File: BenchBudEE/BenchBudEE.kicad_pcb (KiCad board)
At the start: 4 copper layers, 165.1 x 63.5 mm, 0 parts

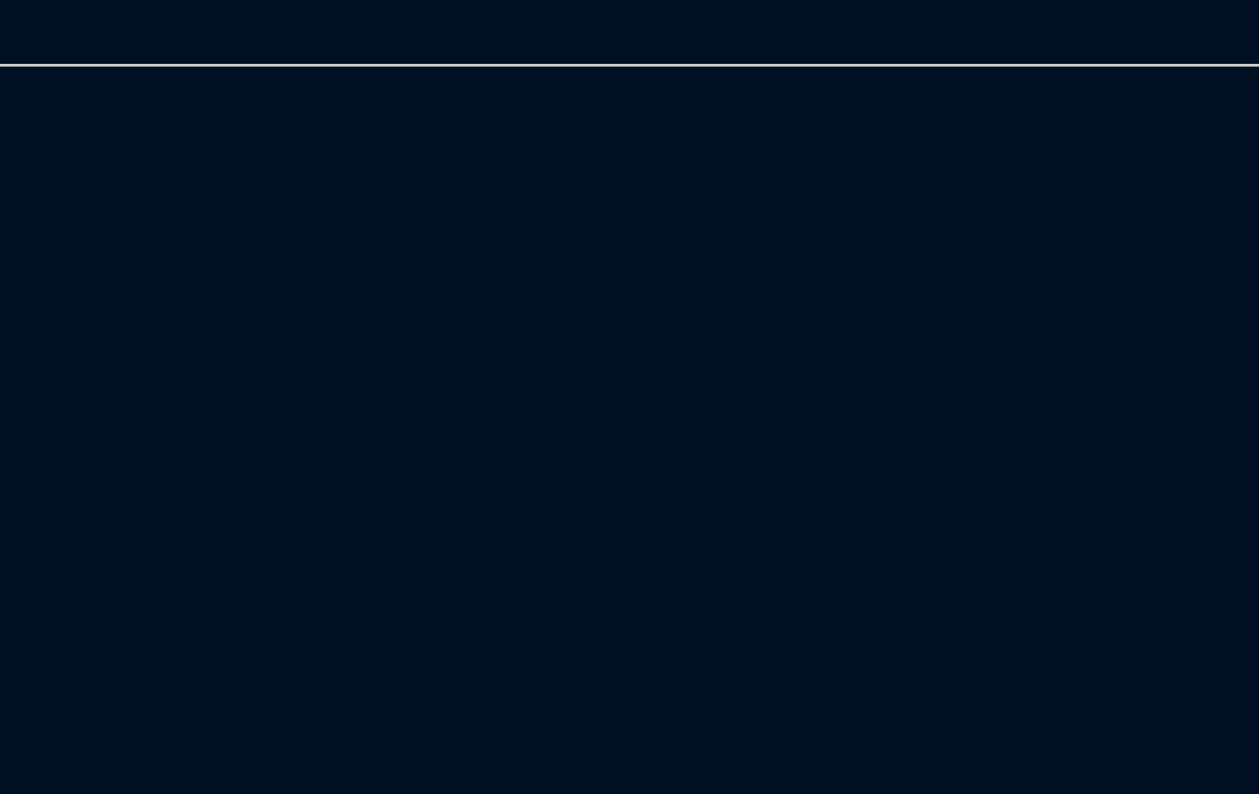
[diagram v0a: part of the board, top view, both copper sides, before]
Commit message: Associating and Placing the Relay Module
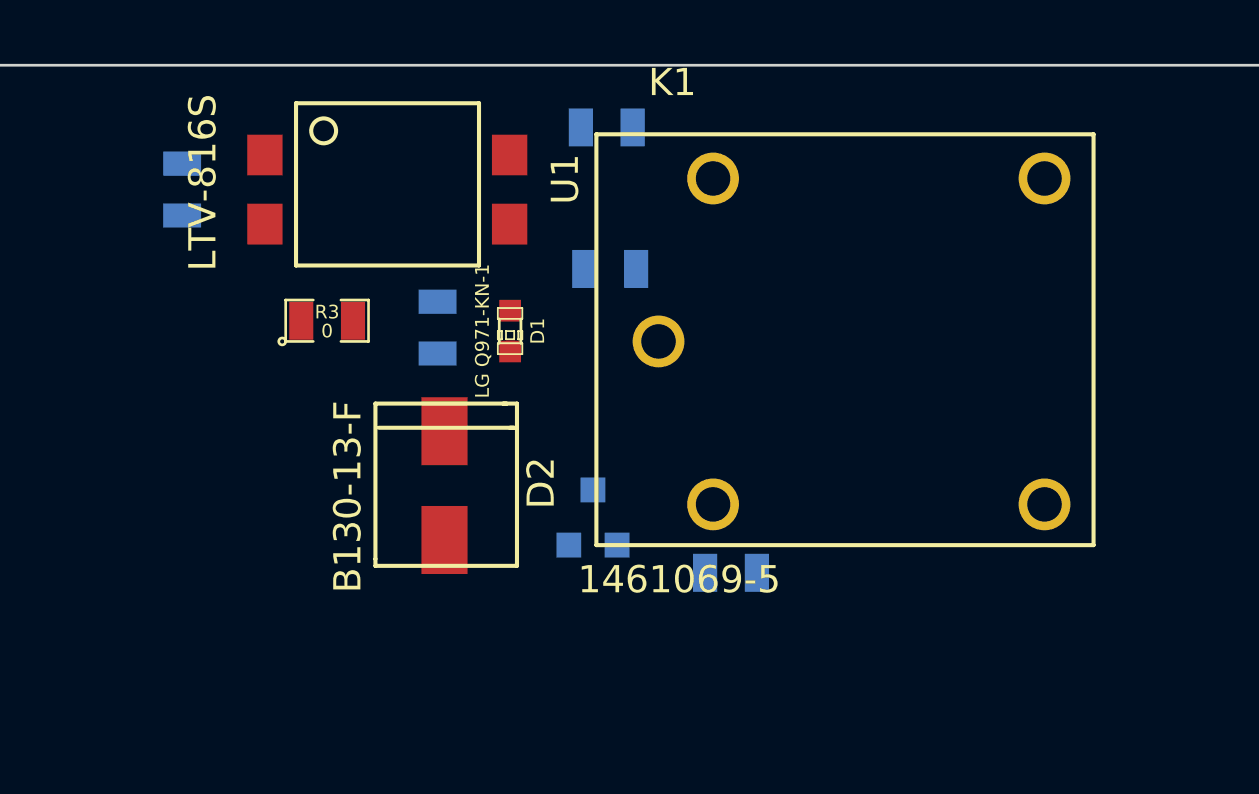
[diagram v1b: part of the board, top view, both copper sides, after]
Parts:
- added D1: LG Q971-KN-1, LED-0603, F.Cu at (252.6, 107.8)
- added D2: B130-13-F, SMA, F.Cu at (250.2, 111.5)
- added K1: 1461069-5, TE-SPDT, F.Cu at (258.1, 108.2)
- added Q1: 2N3904, SOT23EBC, B.Cu at (255.7, 114.7)
- added R1: 500, SM0805, B.Cu at (240.5, 102.6)
- added R2: 200, SM0805, B.Cu at (249.9, 107.7)
- added R3: 0, SM0805, F.Cu at (245.9, 107.4)
- added R4: 100, SM0805, B.Cu at (256.3, 105.5)
- added R5: 0, SM0805, B.Cu at (256.2, 100.3)
- added R6: 0, SM0805, B.Cu at (260.7, 116.7)
- added U1: LTV-816S, 4-SMD, F.Cu at (243.6, 101.3)

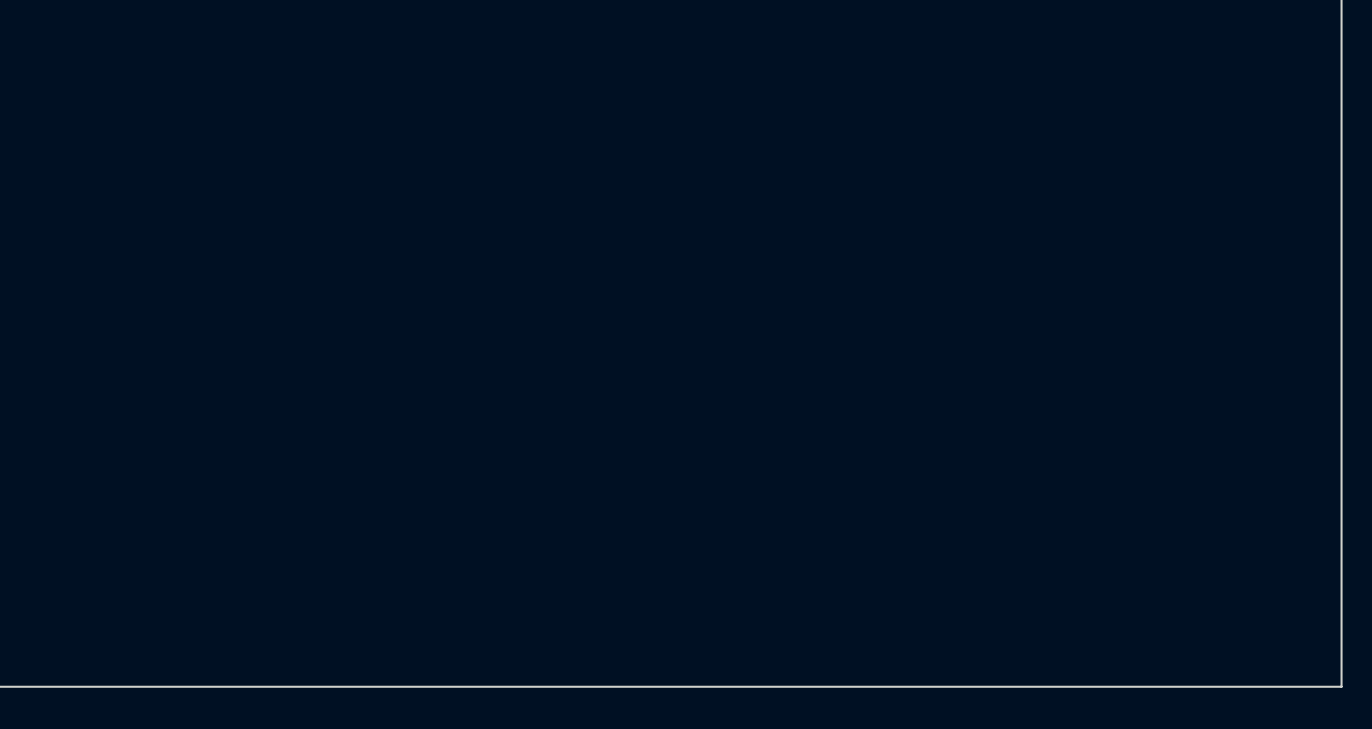
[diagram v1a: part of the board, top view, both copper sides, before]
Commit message: Associating and Placingthe Thermocouple Module
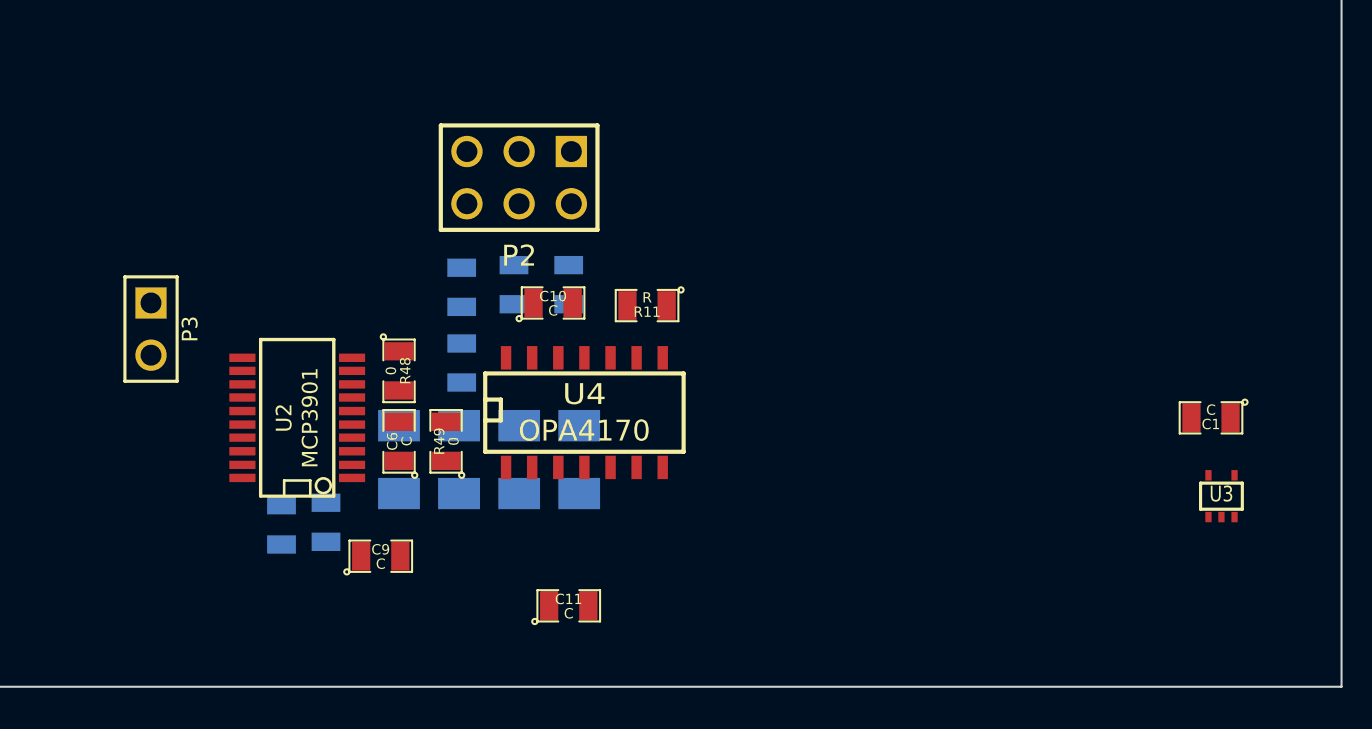
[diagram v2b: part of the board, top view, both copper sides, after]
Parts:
- added C1: C, SM0805, F.Cu at (284.0, 148.5)
- added C10: C, SM0805, F.Cu at (252.0, 142.9)
- added C11: C, SM0805, F.Cu at (252.7, 157.6)
- added C6: C, SM0805, F.Cu at (244.5, 149.6)
- added C7: C, SM0805, B.Cu at (238.8, 153.7)
- added C8: C, SM0805, B.Cu at (240.9, 153.5)
- added C9: C, SM0805, F.Cu at (243.6, 155.2)
- added P2: CONN_3X2, pin_array_3x2, F.Cu at (250.3, 136.8)
- added P3: CONN_2, PIN_ARRAY_2X1, F.Cu at (232.4, 144.1)
- added R10: R, SM1206, B.Cu at (253.2, 150.5)
- added R11: R, SM0805, F.Cu at (256.5, 143.0)
- added R12: R, SM0805, B.Cu at (252.7, 142.0)
- added R13: R, SM0805, B.Cu at (247.5, 145.8)
- added R44: R, SM0805, B.Cu at (247.5, 142.1)
- added R45: R, SM0805, B.Cu at (250.1, 142.0)
- added R48: 0, SM0805, F.Cu at (244.5, 146.2)
- added R49: 0, SM0805, F.Cu at (246.8, 149.6)
- added R7: R, SM1206, B.Cu at (244.5, 150.5)
- added R8: R, SM1206, B.Cu at (247.4, 150.5)
- added R9: R, SM1206, B.Cu at (250.3, 150.5)
- added U2: MCP3901, SSOP20, F.Cu at (239.5, 148.5)
- added U3: LMT84, SOT353, F.Cu at (284.5, 152.3)
- added U4: OPA4170, SO14E, F.Cu at (253.5, 148.1)

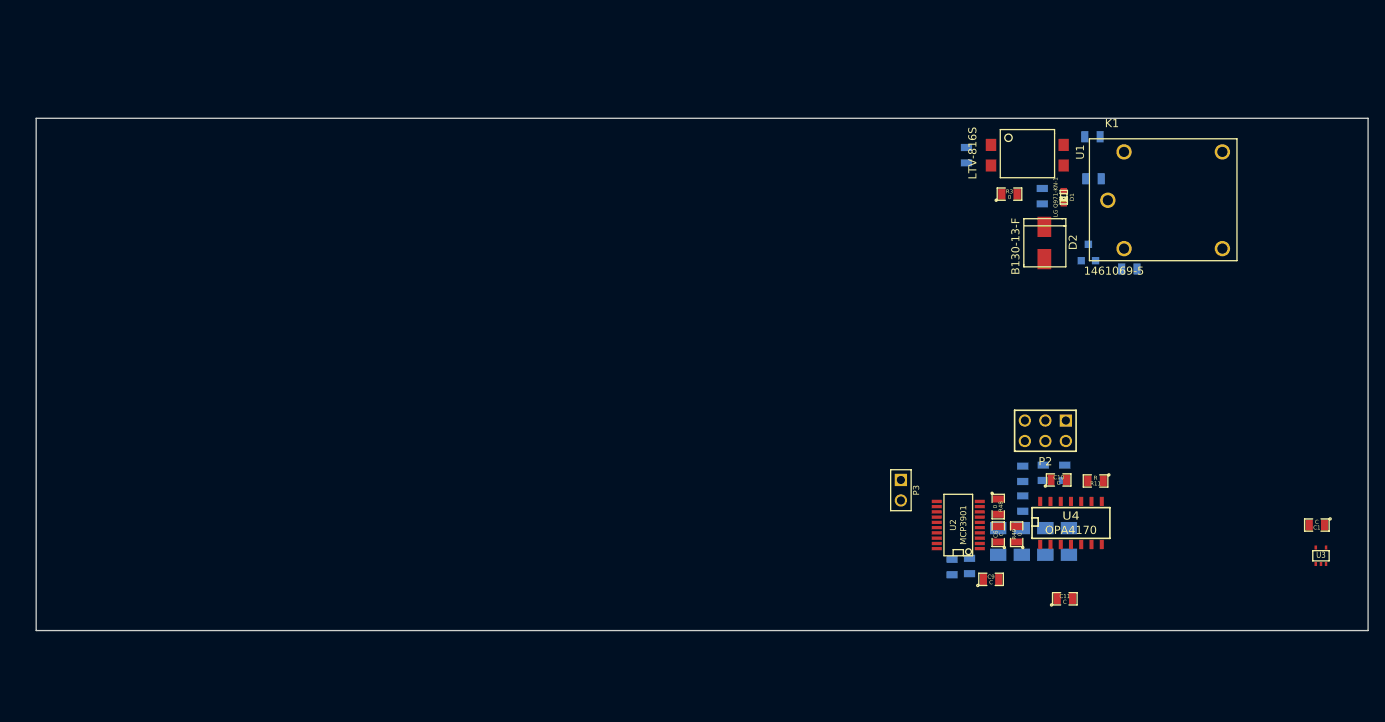
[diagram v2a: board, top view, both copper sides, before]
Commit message: Associating and Placing the Terminal Block Module
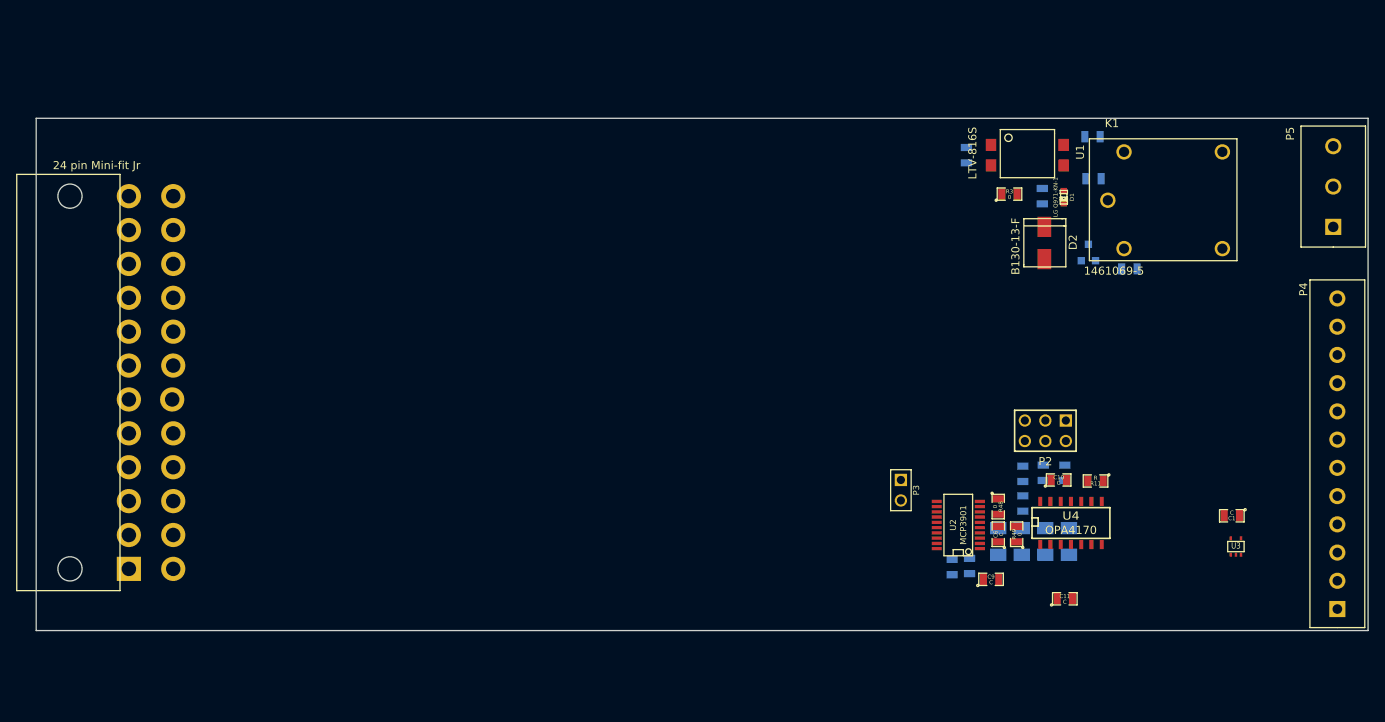
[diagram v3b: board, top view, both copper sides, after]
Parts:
- added P1: 24 pin Mini-fit Jr, ATX_Header, F.Cu at (129.4, 107.7)
- added P4: 12 pin terminal block, 12_Pin_TB, F.Cu at (286.5, 158.9)
- added P5: 3 Pin TB, 3_Pin_TB, F.Cu at (286.0, 111.5)
- moved C1 10.6 mm to (273.4, 147.3)
- moved U3 10.6 mm to (273.9, 151.1)
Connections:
- K1 pad 1: (no net) -> /Relay/RELAY_COM
- K1 pad 3: (no net) -> /Relay/RELAY_NO
- K1 pad 4: (no net) -> /Relay/RELAY_NC

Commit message: Associating and Placing Arduino Block Module
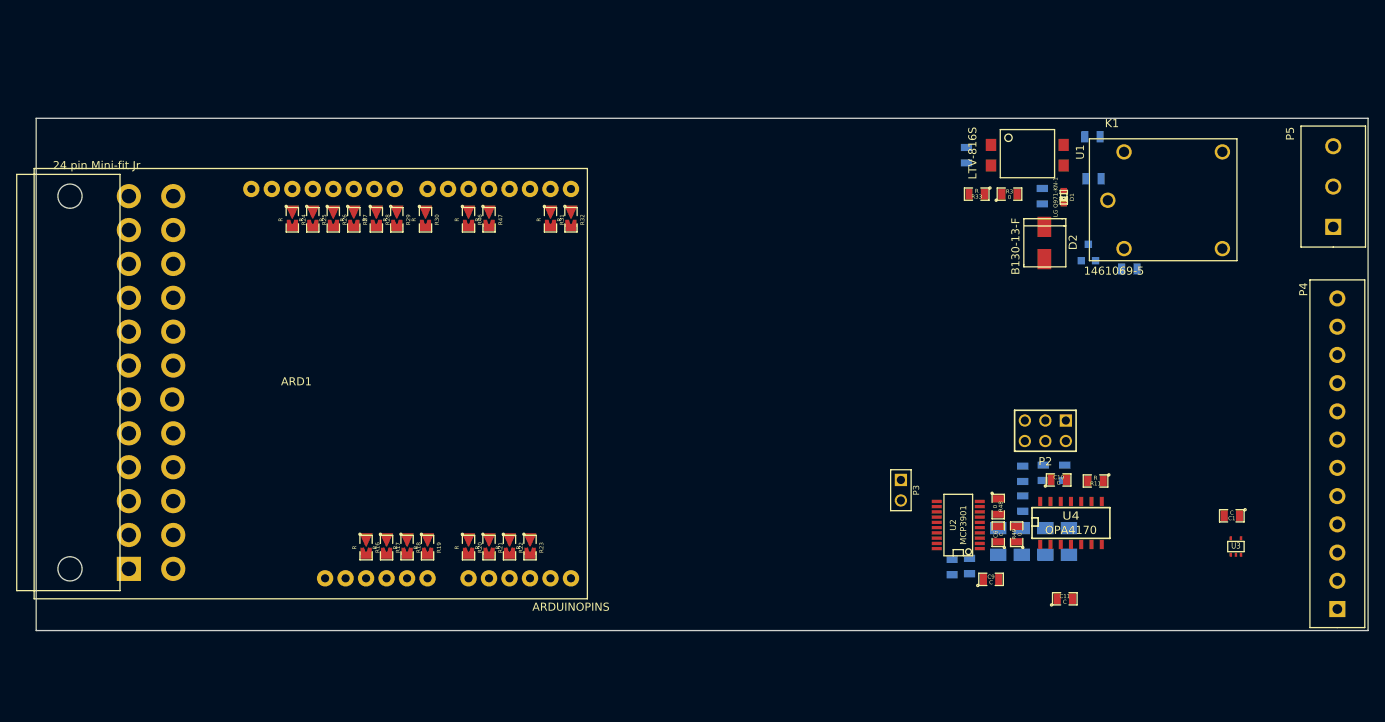
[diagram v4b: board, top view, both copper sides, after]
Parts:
- added ARD1: ARDUINOPINS, Arduino, F.Cu at (157.5, 130.7)
- added R16: R, SM0805-blob, F.Cu at (166.1, 151.3)
- added R17: R, SM0805-blob, F.Cu at (168.7, 151.3)
- added R18: R, SM0805-blob, F.Cu at (171.2, 151.3)
- added R19: R, SM0805-blob, F.Cu at (173.7, 151.3)
- added R20: R, SM0805-blob, F.Cu at (178.8, 151.3)
- added R21: R, SM0805-blob, F.Cu at (181.4, 151.3)
- added R22: R, SM0805-blob, F.Cu at (183.9, 151.3)
- added R23: R, SM0805-blob, F.Cu at (186.4, 151.3)
- added R24: R, SM0805-blob, F.Cu at (157.0, 110.6)
- added R25: R, SM0805-blob, F.Cu at (159.5, 110.6)
- added R26: R, SM0805-blob, F.Cu at (162.1, 110.6)
- added R27: R, SM0805-blob, F.Cu at (164.6, 110.6)
- added R28: R, SM0805-blob, F.Cu at (167.4, 110.6)
- added R29: R, SM0805-blob, F.Cu at (169.9, 110.6)
- added R30: R, SM0805-blob, F.Cu at (173.5, 110.6)
- added R31: R, SM0805-blob, F.Cu at (189.0, 110.6)
- added R32: R, SM0805-blob, F.Cu at (191.5, 110.6)
- added R33: R, SM0805, F.Cu at (241.8, 107.4)
- added R46: R, SM0805-blob, F.Cu at (178.8, 110.6)
- added R47: R, SM0805-blob, F.Cu at (181.4, 110.6)
